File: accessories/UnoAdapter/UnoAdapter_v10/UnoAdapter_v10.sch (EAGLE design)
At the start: 10 parts, among them X1 DC21MMX

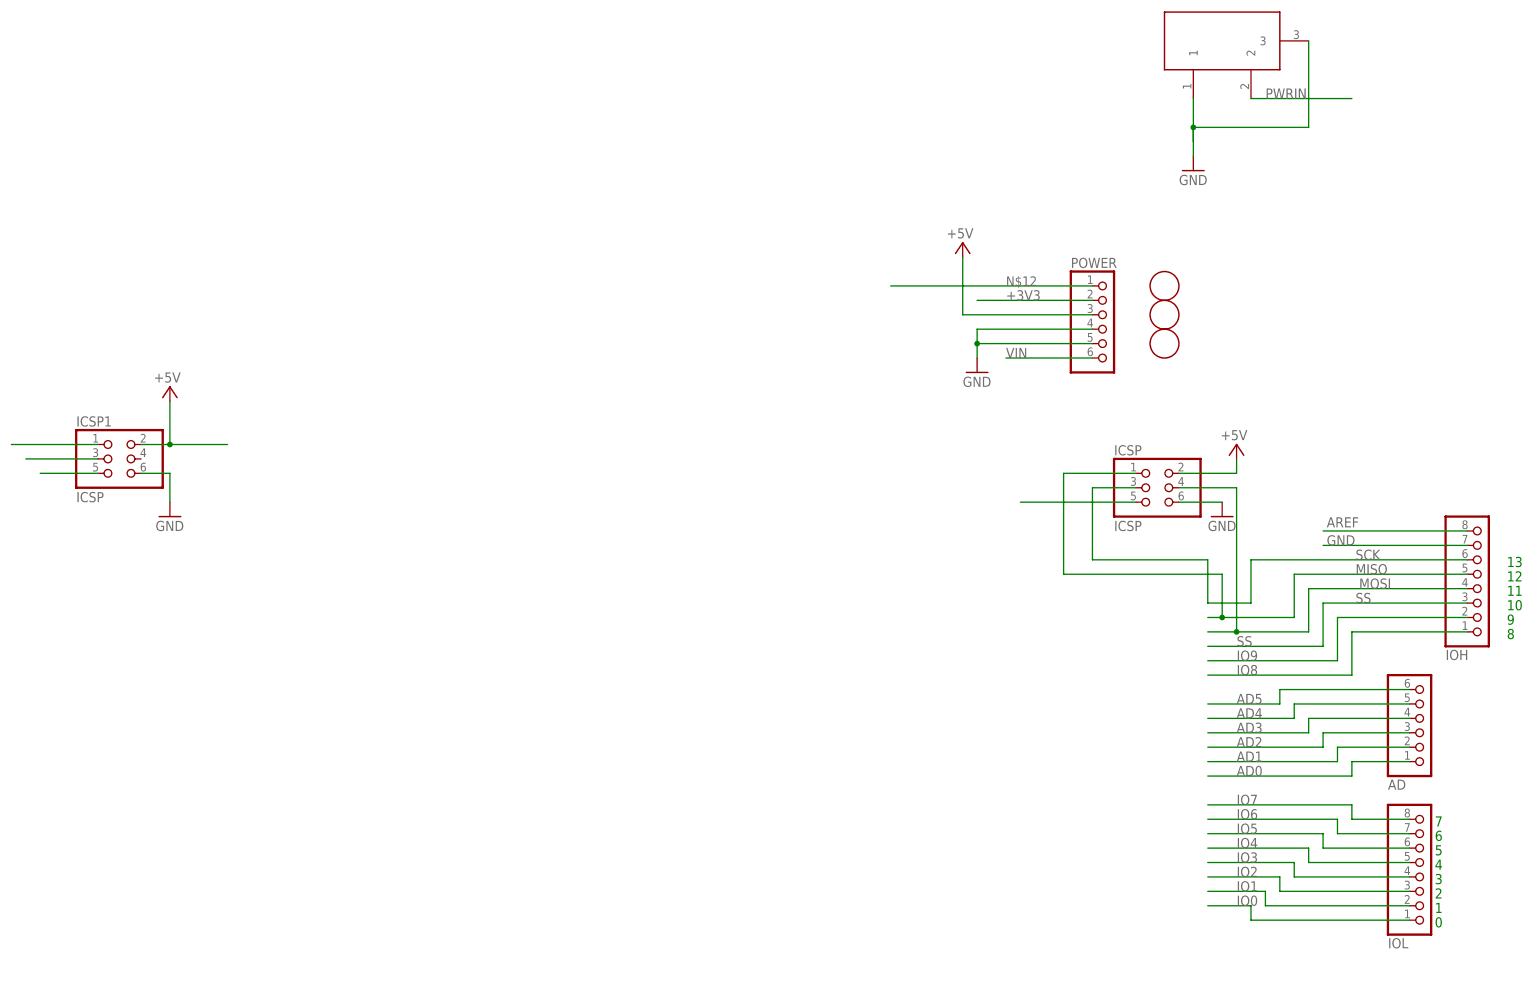
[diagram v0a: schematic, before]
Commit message: More work on Uno Adapter
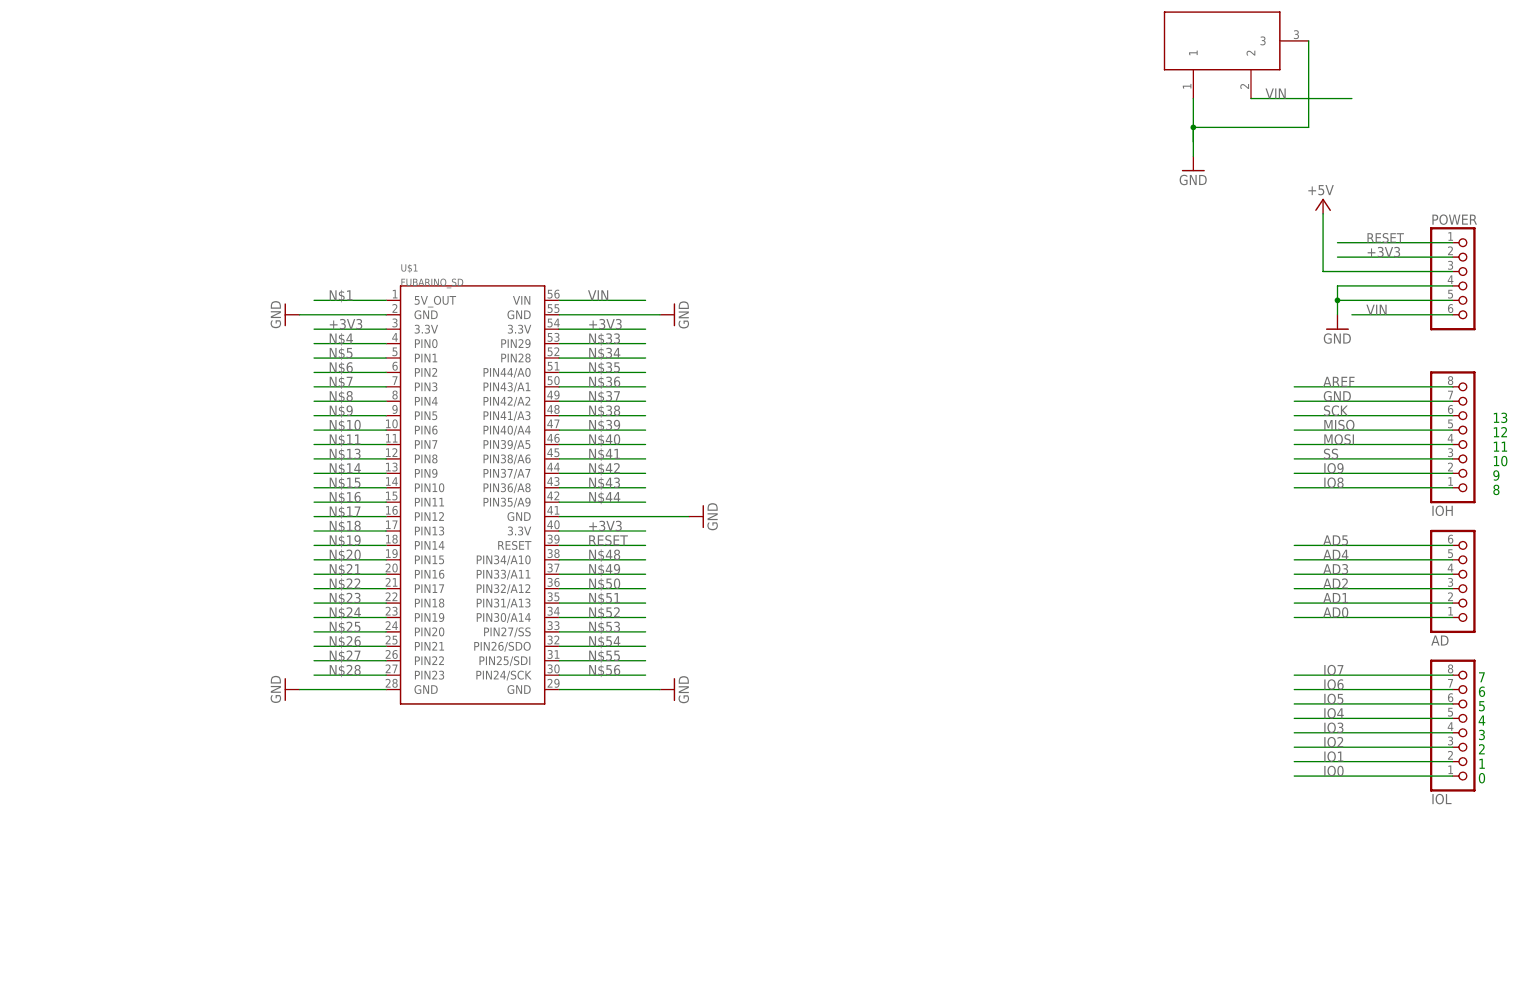
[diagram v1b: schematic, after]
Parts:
- removed ICSP, ICSP1: ICSP, pinhead:PINHD-2X3
- removed U$3, U$4, U$6: FIDUCIALMOUNT, SmartPrj:FIDUCIALMOUNT
- added U$1: FUBARINO_SD, SchmalzHausPublic:FUBARINO_SD
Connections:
- removed net MISO2: ICSP1.1
- removed net N$12: POWER.1
- removed net PWRIN: X1.2
- removed net RESET2: ICSP1.5
- removed net SCK2: ICSP1.3
- new net N$1: U$1.5V_OUT
- new net N$10: U$1.PIN6
- new net N$11: U$1.PIN7
- new net N$13: U$1.PIN8
- new net N$14: U$1.PIN9
- new net N$15: U$1.PIN10
- new net N$16: U$1.PIN11
- new net N$17: U$1.PIN12
- new net N$18: U$1.PIN13
- new net N$19: U$1.PIN14
- new net N$20: U$1.PIN15
- new net N$21: U$1.PIN16
- new net N$22: U$1.PIN17
- new net N$23: U$1.PIN18
- new net N$24: U$1.PIN19
- new net N$25: U$1.PIN20
- new net N$26: U$1.PIN21
- new net N$27: U$1.PIN22
- new net N$28: U$1.PIN23
- new net N$33: U$1.PIN29
- new net N$34: U$1.PIN28
- new net N$35: U$1.PIN44/A0
- new net N$36: U$1.PIN43/A1
- new net N$37: U$1.PIN42/A2
- new net N$38: U$1.PIN41/A3
- new net N$39: U$1.PIN40/A4
- new net N$4: U$1.PIN0
- new net N$40: U$1.PIN39/A5
- new net N$41: U$1.PIN38/A6
- new net N$42: U$1.PIN37/A7
- new net N$43: U$1.PIN36/A8
- new net N$44: U$1.PIN35/A9
- new net N$48: U$1.PIN34/A10
- new net N$49: U$1.PIN33/A11
- new net N$5: U$1.PIN1
- new net N$50: U$1.PIN32/A12
- new net N$51: U$1.PIN31/A13
- new net N$52: U$1.PIN30/A14
- new net N$53: U$1.PIN27/SS
- new net N$54: U$1.PIN26/SDO
- new net N$55: U$1.PIN25/SDI
- new net N$56: U$1.PIN24/SCK
- new net N$6: U$1.PIN2
- new net N$7: U$1.PIN3
- new net N$8: U$1.PIN4
- new net N$9: U$1.PIN5
- net +3V3: now also U$1.3.3V@1, U$1.3.3V@2, U$1.3.3V@3
- net +5V: no longer ICSP.2, ICSP1.2
- net GND: now also U$1.GND@1, U$1.GND@2, U$1.GND@3, U$1.GND@4, U$1.GND@5; no longer ICSP.6, ICSP1.6
- net MISO: no longer ICSP.1
- net MOSI: no longer ICSP.4
- net RESET: now also POWER.1, U$1.RESET; no longer ICSP.5
- net SCK: no longer ICSP.3
- net VIN: now also U$1.VIN, X1.2
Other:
- note added: "Fubarino Arduino Uno Adapter Board"
- moved on the sheet: AD, IOH, IOL, POWER

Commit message: Added Fubarino Mini to board.
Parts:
- added U$2: FUBARINO_MINI, SchmalzHausPublic:FUBARINO_MINI
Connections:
- removed net N$1: U$1.5V_OUT
- new net N$30: U$2.PIN32
- new net N$31: U$2.PIN31
- new net N$32: U$2.PIN30
- new net N$45: U$2.PIN29
- new net N$46: U$2.PIN28
- new net N$47: U$2.PIN27
- new net N$57: U$2.PIN26
- new net N$58: U$2.PIN25
- new net N$59: U$2.PIN24
- new net N$60: U$2.PIN23
- new net N$61: U$2.PIN22
- new net N$62: U$2.PIN21
- new net N$63: U$2.PIN20/A12
- new net N$64: U$2.PIN19
- new net N$65: U$2.PIN18
- new net N$66: U$2.PIN17
- new net N$70: U$2.PIN0/A0
- new net N$71: U$2.PIN1
- new net N$72: U$2.PIN2
- new net N$73: U$2.PIN3/A1
- new net N$74: U$2.PIN4/A2
- new net N$75: U$2.PIN5/A3
- new net N$76: U$2.PIN6/A4
- new net N$77: U$2.PIN7/A5
- new net N$78: U$2.PIN8/A6
- new net N$79: U$2.PIN9/A7
- new net N$80: U$2.PIN10/A8
- new net N$81: U$2.PIN11/A9
- new net N$82: U$2.PIN12/A10
- new net N$83: U$2.PIN13/A11
- new net N$84: U$2.PIN14
- new net N$85: U$2.PIN15
- new net N$86: U$2.PIN16
- net +3V3: now also U$2.3.3V@1, U$2.3.3V@3
- net +5V: now also U$1.5V_OUT, U$2.5V_OUT
- net GND: now also U$2.GND@1, U$2.GND@4, U$2.GND@5
- net VIN: now also U$2.VIN

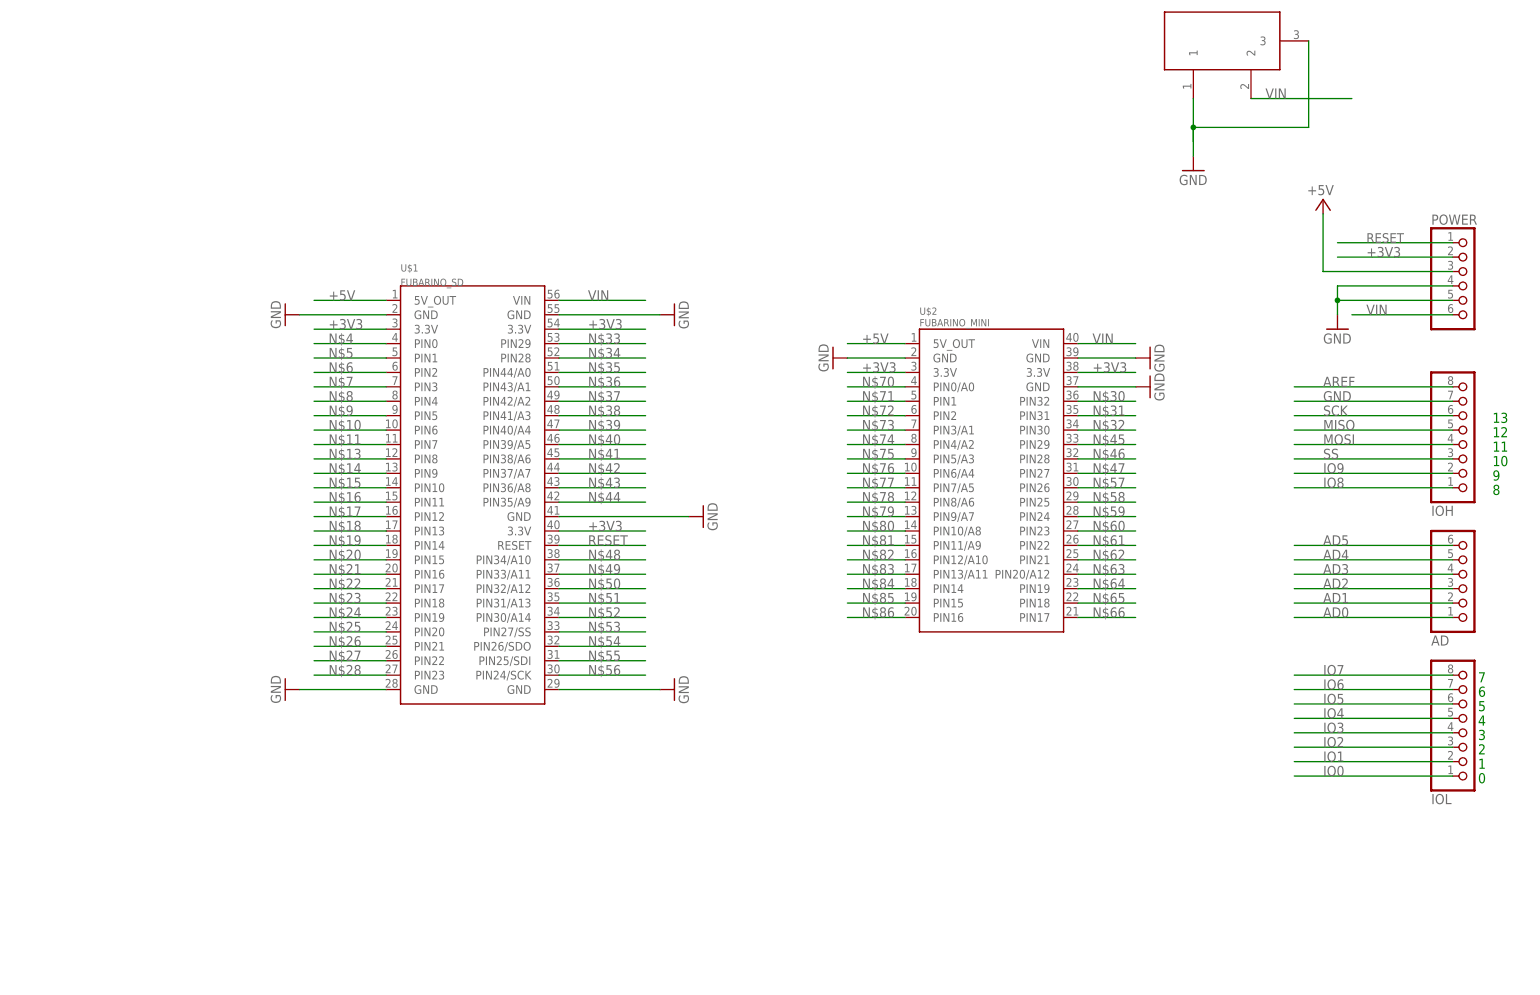
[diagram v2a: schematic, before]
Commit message: Moved Fubarinos around, added regulator.
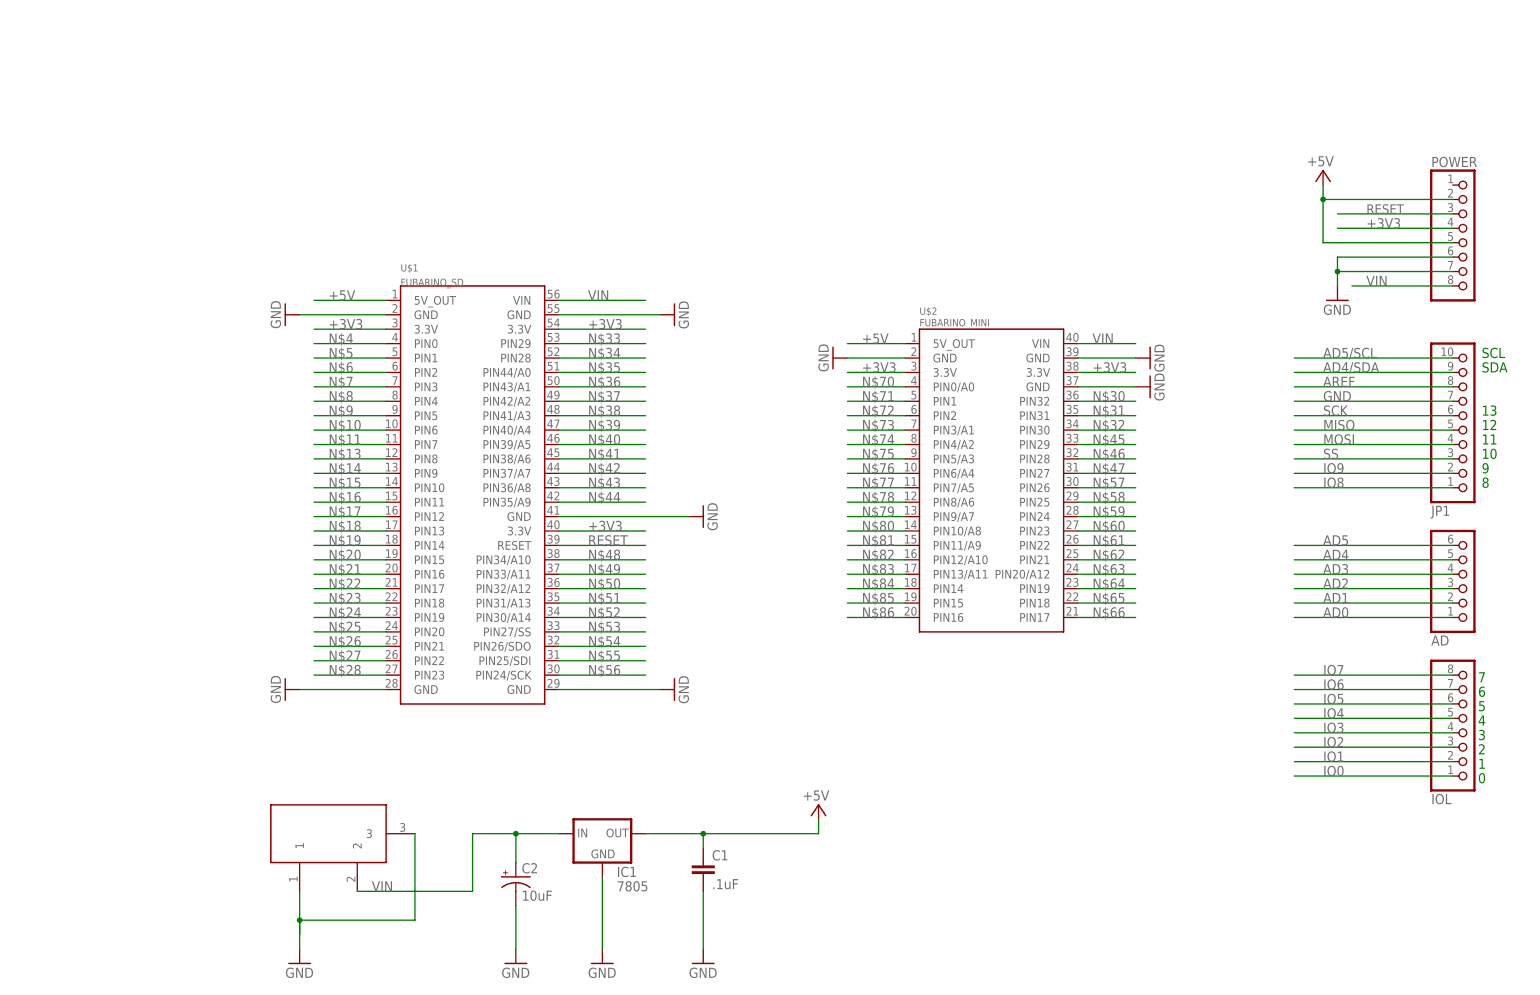
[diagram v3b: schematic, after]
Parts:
- removed IOH: (no value), pinhead:PINHD-1X8
- added C1: .1uF, SparkFun-Capacitors:CAPPTH
- added C2: 10uF, SparkFun-Capacitors:CAP_POLPTH2
- added IC1: 7805, SparkFun-PowerIC:V_REG_78XXSIDE
- added JP1: (no value), pinhead:PINHD-1X10
- POWER: device pinhead:PINHD-1X6 -> pinhead:PINHD-1X8
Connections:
- new net AD4/SDA: JP1.9
- new net AD5/SCL: JP1.10
- net +3V3: now also POWER.4; no longer POWER.2
- net +5V: now also C1.1, IC1.OUT, POWER.2, POWER.5; no longer POWER.3
- net AREF: now also JP1.8; no longer IOH.8
- net GND: now also C1.2, C2.-, IC1.GND, JP1.7, POWER.6, POWER.7; no longer IOH.7, POWER.4, POWER.5
- net IO8: now also JP1.1; no longer IOH.1
- net IO9: now also JP1.2; no longer IOH.2
- net MISO: now also JP1.5; no longer IOH.5
- net MOSI: now also JP1.4; no longer IOH.4
- net RESET: now also POWER.3; no longer POWER.1
- net SCK: now also JP1.6; no longer IOH.6
- net SS: now also JP1.3; no longer IOH.3
- net VIN: now also C2.+, IC1.IN, POWER.8; no longer POWER.6
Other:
- note added: "SCL"
- note added: "SDA"

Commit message: Got some more work done on the board - fixed power issues, added reset/prg switches, moved Fubarinos inside Uno headers.
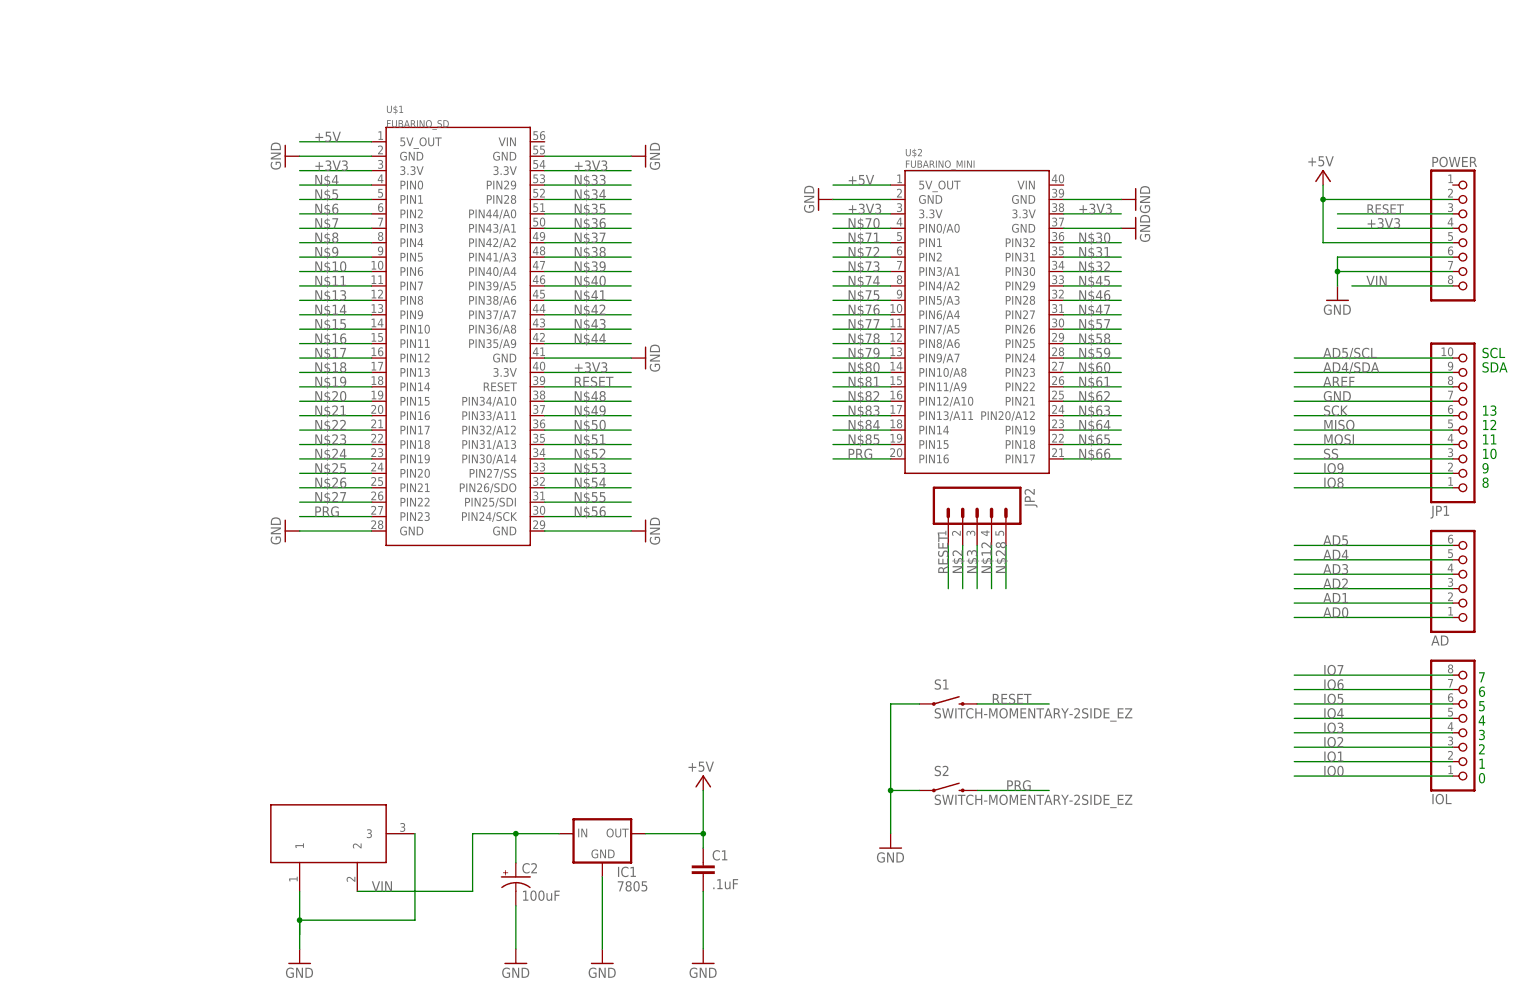
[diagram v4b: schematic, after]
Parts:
- added JP2: (no value), SparkFun-Connectors:M05PTH
- added S1, S2: SWITCH-MOMENTARY-2SIDE_EZ, SparkFun-Electromechanical:SWITCH-MOMENTARY-2SIDE_EZ
- C2: value 10uF -> 100uF; device SparkFun-Capacitors:CAP_POLPTH2 -> SparkFun-Capacitors:CAP_POLPTH1
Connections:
- removed net N$86: U$2.PIN16
- new net N$12: JP2.4
- new net N$2: JP2.2
- new net N$3: JP2.3
- new net PRG: S2.2, U$1.PIN23, U$2.PIN16
- net GND: now also S1.1, S2.1
- net N$28: now also JP2.5; no longer U$1.PIN23
- net RESET: now also JP2.1, S1.2
- net VIN: no longer U$1.VIN, U$2.VIN
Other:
- moved on the sheet: U$1, U$2
